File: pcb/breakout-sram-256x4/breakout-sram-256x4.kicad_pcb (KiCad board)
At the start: 6 copper layers, 100 x 51.2 mm, 26 parts, among them J1 DF40C-100DS-0.4V51, J10 DF40C-40DP-0.4V51, J2 DF40C-100DS-0.4V51, J3 DF40C-100DS-0.4V51, J4 DF40C-100DS-0.4V51, J5 DF40C-100DP-0.4V51, J6 DF40C-100DP-0.4V51, J7 DF40C-100DP-0.4V51, J8 DF40C-100DP-0.4V51, J9 DF40C-40DS-0.4V51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

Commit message: [sram_4x][pcb] make each sram ce settable with 0 ohm 603s
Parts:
- added R1: 10K, Resistor_SMD:R_0603_1608Metric, F.Cu at (89.4, 58.5)
- added R2: 0, Resistor_SMD:R_0603_1608Metric, F.Cu at (89.4, 60.6)
- added R3: 10K, Resistor_SMD:R_0603_1608Metric, F.Cu at (89.4, 81.8)
- added R4: 0, Resistor_SMD:R_0603_1608Metric, F.Cu at (89.4, 83.7)
- added R5: 10K, Resistor_SMD:R_0603_1608Metric, F.Cu at (96.4, 58.5)
- added R6: 0, Resistor_SMD:R_0603_1608Metric, F.Cu at (96.4, 60.6)
- added R7: 10K, Resistor_SMD:R_0603_1608Metric, F.Cu at (96.4, 81.8)
- added R8: 0, Resistor_SMD:R_0603_1608Metric, F.Cu at (96.4, 83.7)
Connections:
- U1 pad 6: GND -> /U1_CEn
- U2 pad 6: GND -> /U2_CEn
- U3 pad 6: GND -> /U3_CEn
- U4 pad 6: GND -> /U4_CEn
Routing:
- net /U2_CEn: track 0.00 -> 32.5 mm, vias 0 -> 2
- net /U1_CEn: track 0.00 -> 22.2 mm, vias 0 -> 2
- net /U4_CEn: track 0.00 -> 11.5 mm
- net /U3_CEn: track 0.00 -> 11.4 mm
- net +3V3: track 50.4 -> 55.4 mm, vias 19 -> 23
- net GND: track 376.4 -> 375.6 mm

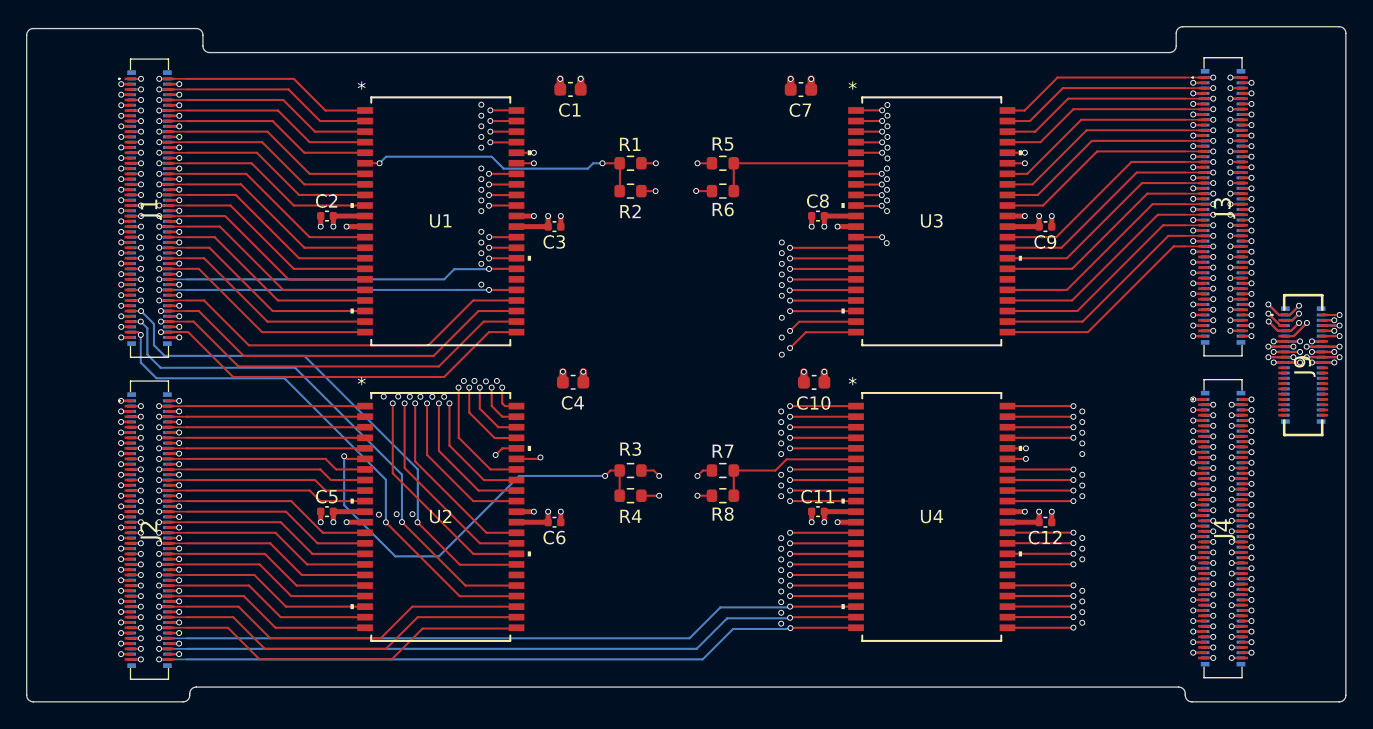
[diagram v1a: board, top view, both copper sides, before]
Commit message: [sram_4x][pcb] do not use nc from ice40
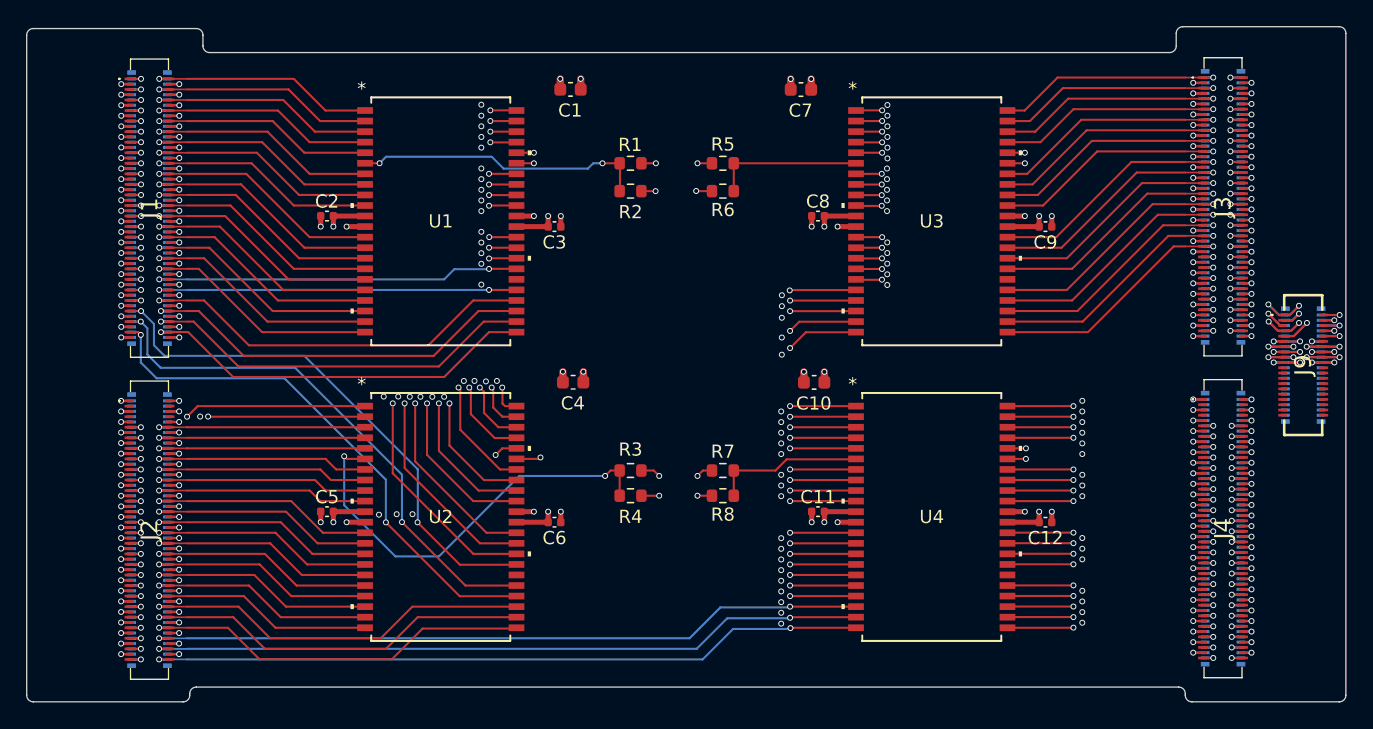
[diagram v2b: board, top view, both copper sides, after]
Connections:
- J2 pad 3: B_3 -> unconnected-(J2-Pad3)
- J2 pad 4: B_4 -> unconnected-(J2-Pad4)
- J2 pad 7: B_7 -> unconnected-(J2-Pad7)
- J2 pad 8: B_8 -> unconnected-(J2-Pad8)
- J4 pad 3: D_3 -> unconnected-(J4-Pad3)
- J4 pad 4: D_4 -> unconnected-(J4-Pad4)
- J4 pad 7: D_7 -> unconnected-(J4-Pad7)
- J4 pad 8: D_8 -> unconnected-(J4-Pad8)
- J6 pad 3: B_4 -> unconnected-(J6-Pad3)
- J6 pad 4: B_3 -> unconnected-(J6-Pad4)
- J6 pad 7: B_8 -> unconnected-(J6-Pad7)
- J6 pad 8: B_7 -> unconnected-(J6-Pad8)
- J8 pad 3: D_4 -> unconnected-(J8-Pad3)
- J8 pad 4: D_3 -> unconnected-(J8-Pad4)
- J8 pad 7: D_8 -> unconnected-(J8-Pad7)
- J8 pad 8: D_7 -> unconnected-(J8-Pad8)
- U2 pad 1: B_4 -> B_11
- U2 pad 2: B_8 -> B_15
- U3 pad 14: B_3 -> C_42
- U3 pad 15: B_7 -> C_46
- U3 pad 16: B_11 -> C_50
- U3 pad 17: B_15 -> C_54
- U4 pad 23: D_68 -> D_76
- U4 pad 24: D_64 -> D_72
- U4 pad 25: D_60 -> D_68
- U4 pad 26: D_56 -> D_64
- U4 pad 27: D_52 -> D_60
- U4 pad 29: D_48 -> D_56
- U4 pad 30: D_44 -> D_52
- U4 pad 31: D_40 -> D_48
- U4 pad 32: D_36 -> D_44
- U4 pad 35: D_32 -> D_40
- U4 pad 36: D_28 -> D_36
- U4 pad 37: D_24 -> D_32
- U4 pad 38: D_20 -> D_28
- U4 pad 41: D_16 -> D_24
- U4 pad 42: D_12 -> D_20
- U4 pad 43: D_8 -> D_16
- U4 pad 44: D_4 -> D_12
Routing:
- net B_3: track 61.6 -> 0.00 mm, vias 2 -> 0
- net B_7: track 61.5 -> 0.00 mm, vias 2 -> 0
- net B_15: track 61.6 -> 19.3 mm
- net B_11: track 61.5 -> 19.3 mm
- net C_50: track 1.62 -> 32.7 mm, vias 1 -> 2
- net C_46: track 1.62 -> 32.7 mm, vias 1 -> 2
- net C_54: track 1.62 -> 32.7 mm, vias 1 -> 2
- net C_42: track 1.62 -> 32.7 mm, vias 1 -> 2
- net D_8: track 19.3 -> 0.00 mm, vias 2 -> 0
- net D_4: track 19.3 -> 0.00 mm, vias 2 -> 0
- net D_76: track 1.62 -> 20.3 mm, vias 1 -> 2
- net D_72: track 1.62 -> 20.3 mm, vias 1 -> 2
- net B_8: track 16.2 -> 0.00 mm, vias 1 -> 0
- net B_4: track 16.2 -> 0.00 mm, vias 1 -> 0
- net D_7: track 1.39 -> 0.00 mm, vias 1 -> 0
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
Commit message: [sram_4x][pcb] use bottom of lower right bank
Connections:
- U4 pad 23: D_76 -> D_100
- U4 pad 24: D_72 -> D_96
- U4 pad 25: D_68 -> D_92
- U4 pad 26: D_64 -> D_88
- U4 pad 27: D_60 -> D_84
- U4 pad 29: D_56 -> D_80
- U4 pad 30: D_52 -> D_76
- U4 pad 31: D_48 -> D_72
- U4 pad 32: D_44 -> D_68
- U4 pad 35: D_40 -> D_64
- U4 pad 36: D_36 -> D_60
- U4 pad 37: D_32 -> D_56
- U4 pad 38: D_28 -> D_52
- U4 pad 41: D_24 -> D_48
- U4 pad 42: D_20 -> D_44
- U4 pad 43: D_16 -> D_40
- U4 pad 44: D_12 -> D_36
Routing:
- net D_80: track 1.62 -> 19.9 mm, vias 1 -> 2
- net D_100: track 1.62 -> 19.6 mm, vias 1 -> 2
- net D_84: track 1.62 -> 19.5 mm, vias 1 -> 2
- net D_88: track 1.62 -> 19.5 mm, vias 1 -> 2
- net D_92: track 1.62 -> 19.5 mm, vias 1 -> 2
- net D_96: track 1.62 -> 19.5 mm, vias 1 -> 2
- net D_12: track 19.3 -> 1.62 mm, vias 2 -> 1
- net D_28: track 19.3 -> 1.62 mm, vias 2 -> 1
- net D_32: track 19.3 -> 1.62 mm, vias 2 -> 1
- net D_16: track 19.2 -> 1.62 mm, vias 2 -> 1
- net D_24: track 19.2 -> 1.62 mm, vias 2 -> 1
- net D_20: track 19.2 -> 1.62 mm, vias 2 -> 1
- net D_40: track 19.3 -> 21.2 mm
- net D_36: track 19.3 -> 21.2 mm
- net D_44: track 20.0 -> 21.2 mm
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
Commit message: [sram_4x][pcb] fix A_25 net label
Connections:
- net A_23 renamed A_25

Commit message: [sram_4x][pcb] fix C_25 net label
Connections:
- net C_23 renamed C_25
